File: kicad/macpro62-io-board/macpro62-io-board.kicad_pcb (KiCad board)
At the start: 6 copper layers, 101 x 173.6 mm, 165 parts, among them J1 IOB-HS1 MCIO 124 RA <- CB J3 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, J2 DISPLAY-LINK MCIO 74 RA <- Fa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, J25 ETH1 i226-V #1: ZJLQ-RJ45-SMD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, J26 ETH2 i226-V #2: ZJLQ-RJ45-SMD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, J28 Stock audio module connector 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, J29 Speaker 2P (stock lead; pitch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, J3 Stock PSU DC-out 12P (UNCONFI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, J30 Optional stock/remote power b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, J31 I/O-wall (821-2222) flex ZIF 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, J4 Stock PSU signal 6P (UNCONFIR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, J5 PSU pass-through -> BP J2 (12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, J6 IOB-LINK GH15 <- BP J6, J7 CONN_C fan + AirPort 2x20 @0.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, J8 Fan-assembly antenna coax: U.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, J9 Optional antenna pass-through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, SW1 DNP with the stock 821-2222-A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, SW2 DIAG button, T1 ETH1 2.5G magnetics JASN V24P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, T2 ETH2 2.5G magnetics JASN V24P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, U1 TPS65994AD PD #1 (C1, C2), U11 TUSB1046A C1 alt-mode mux/red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, U12 TUSB1046A C2 alt-mode mux/red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, U13 TUSB1046A C3 alt-mode mux/red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, U14 TUSB1046A C4 alt-mode mux/red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, U15 TUSB1046A C5 alt-mode mux/red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, U16 TUSB1046A C6 alt-mode mux/red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, U2 TPS65994AD PD #2 (C3, C4), U21 TUSB1002A A1 10G redriver, U22 TUSB1002A A2 10G redriver, U23 TUSB1002A A3 10G redriver, U24 TUSB1002A A4 10G redriver, U25 USB-A A1 VBUS switch 1.5 A (S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, U26 USB-A A2 VBUS switch 1.5 A (S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, U27 USB-A A3 VBUS switch 1.5 A (S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, U28 USB-A A4 VBUS switch 1.5 A (S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, U3 TPS65994AD PD #3 (C5, C6), U30 Hall A (DRV5032 class) - posi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, U31 Hall B (DRV5032 class) - posi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, U32 CH334F hub H1b (C4-C6 + codec), U33 CH334F hub H2 (A1-A4) <- IOB-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, U34 CH334F hub H1a (C1-C3 + H1b) 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, U35 CH334F hub H3 on H2 port 4: A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, U4 PD #1 config SPI flash (W25Q8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, U40 TPS259824ON eFuse 12 V in (15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, U41 TPS56C215 5V_C buck (USB-C VB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, U42 TPS56C215 5V_A buck (USB-A VB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, U43 TLV62585 3V3 (3 A) from 5V_SYS, U50 i226-V 2.5GbE (PCIe x1 from H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, U51 i226-V NVM SPI flash (size pe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, U52 i226-V #2 2.5GbE (PCIe x1 fro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, U53 i226-V #2 NVM SPI flash, U6 PD #2 config SPI flash, U60 TDP158 HDMI 2.0 retimer (GPU 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, U61 1V1 LDO (TDP158 core), U7 PD #3 config SPI flash, U70 C-Media CM108B USB audio code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, U71 PAM8302A mono class-D 2.5 W (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, U80 TLC59116 16-ch I2C LED driver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, U81 LIS2DH12 accelerometer (rotat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, U82 BL24C64A IOB ID EEPROM @0x51, U83 TCA9517 I2C buffer (I2C_SYS <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, U84 74LVC1G07 PD_INT -> IOB_INT_N, U90 EMC2101 fan controller @0x4C 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, U91 ASM1182e PCIe Gen2 switch: up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, U95 TCA9548A @0x70: module ID I2C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, U96 TCA9548A @0x71: module ID I2C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, U97 TCA9555 @0x27 on U96 ch3 (pri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, Y1 12 MHz hub crystal, Y2 12 MHz hub crystal, Y3 12 MHz hub crystal, Y4 25 MHz (i226-V), Y5 12 MHz (CM108B), Y6 25 MHz (i226-V #2), Y7 12 MHz hub crystal (H3)

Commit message: Plate test-print fixes (corners +1mm Y, C2 post -1mm, C1 removed); USB-A/HDMI hand fan-out 0 skew; real DF40 + HDMI footprints
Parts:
- JM1, JM10, JM11, JM2, JM3, JM4, JM5, JM6, JM7, JM8, JM9: footprint MP62_IO:MP62_Hirose_DF40C-50DS-0.4V_PLACEHOLDER -> MP62_IO:MP62_Hirose_DF40C-50DS-0.4V
- moved D226 0.53 mm to (78.3, 92.9)
- moved D227 0.53 mm to (74.9, 92.9)
- moved D228 0.53 mm to (71.5, 92.9)
- moved JM11 0.53 mm to (74.9, 92.9)
- moved U60 0.53 mm to (74.9, 88.4)
- moved U61 0.53 mm to (79.9, 88.4)
- moved D219 0.24 mm to (95.8, 154.8)
- moved D221 0.24 mm to (95.8, 167.5)
- moved D222 0.24 mm to (79.5, 157.4)
- moved D223 0.24 mm to (76.1, 157.4)
- moved D224 0.24 mm to (79.5, 167.5)
- moved D225 0.24 mm to (76.1, 167.5)
- moved JM10 0.24 mm to (77.8, 167.5)
- moved JM7 0.24 mm to (97.5, 157.4)
- moved JM8 0.24 mm to (97.5, 167.5)
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
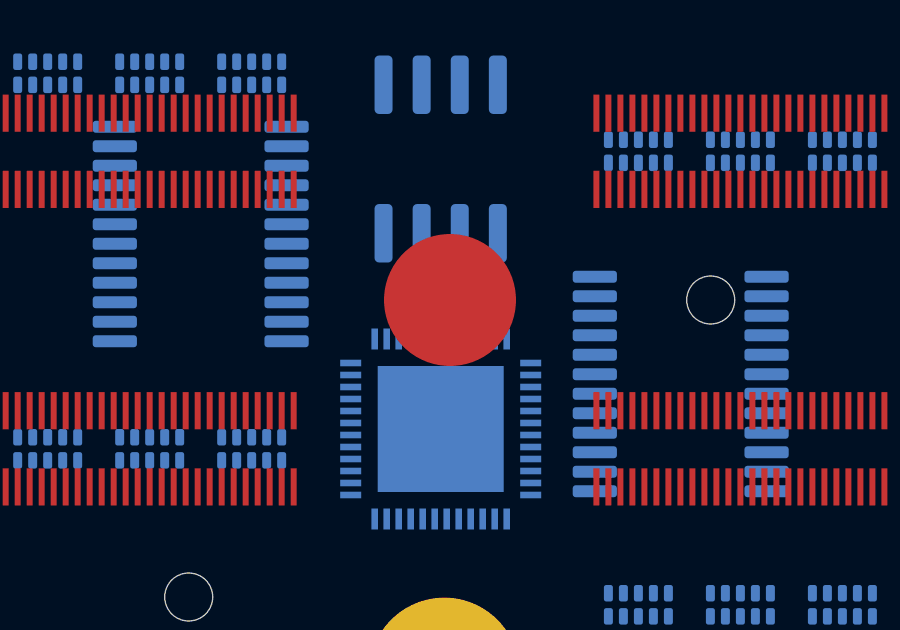
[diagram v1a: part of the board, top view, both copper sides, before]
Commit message: AM5 CPU board draft (parallel to LGA1700); plate: centre post swap, power-button features; H21 moved to Y69.8
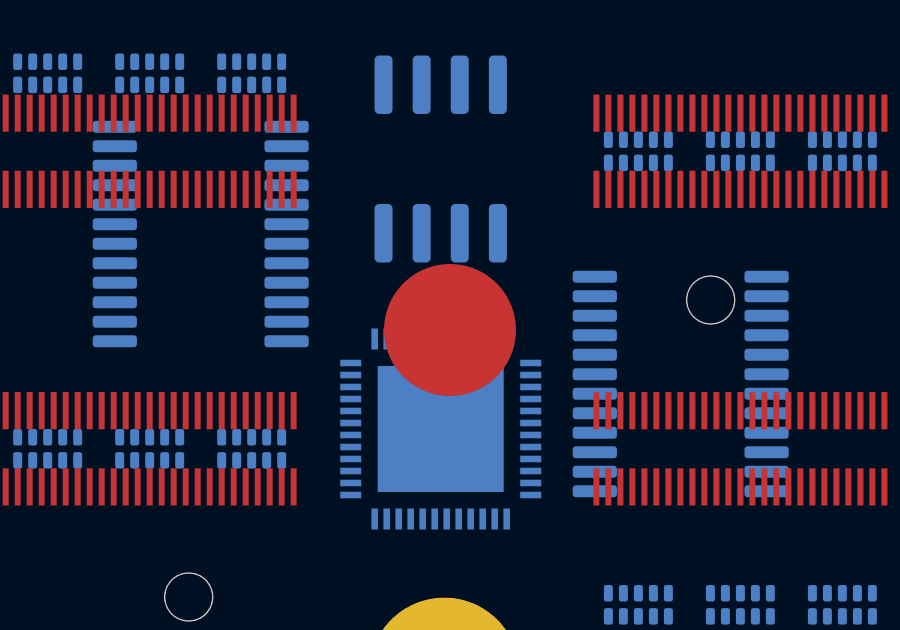
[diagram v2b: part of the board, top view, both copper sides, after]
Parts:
- moved H21 1.00 mm to (87.8, 130.2)

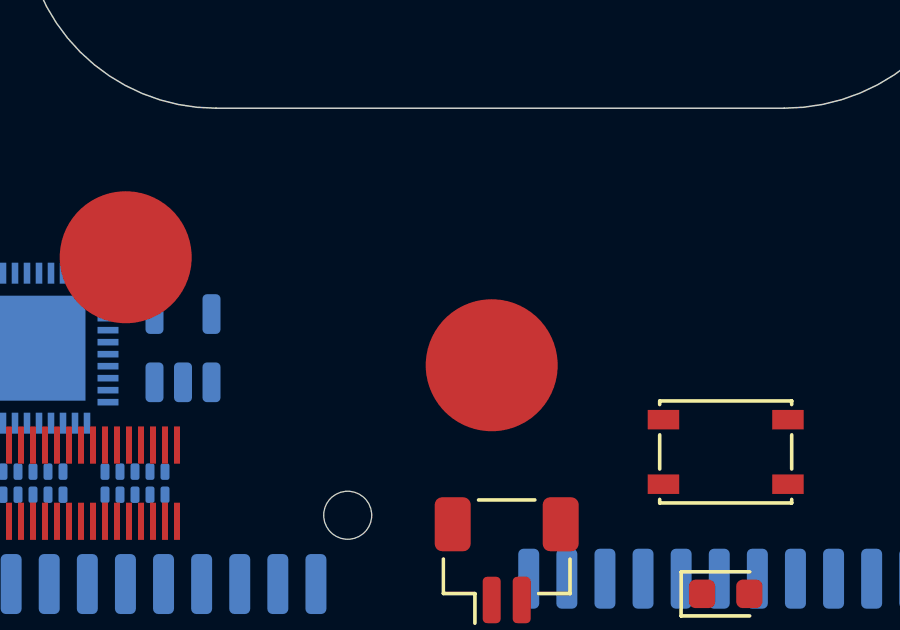
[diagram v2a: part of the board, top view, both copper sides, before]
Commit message: I/O plate: collar + corner-screw fix, print-scan fixes (width, fillets, audio holes, button bosses), HDMI clamp post H25 move, countersunk M2 clamp screws
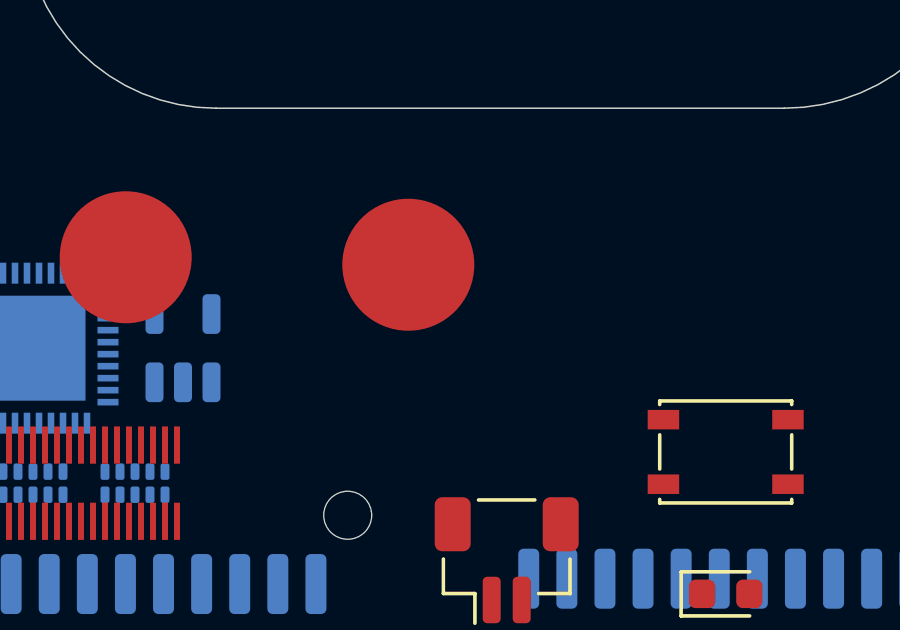
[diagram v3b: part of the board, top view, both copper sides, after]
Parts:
- moved H25 4.35 mm to (87.4, 85.7)
